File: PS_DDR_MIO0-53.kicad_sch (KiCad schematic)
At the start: 1 part, among them U13 XCZU15EG-2FFVB1156E

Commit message: Stuff
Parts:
- removed U13: XCZU15EG-2FFVB1156E, lib:FFVB1156_XIL-L, symbol XCZU15EG:XCZU15EG-2FFVB1156E
- added U13: XCZU15EG-2FFVB1156E, lib:FFVB1156_XIL-L, symbol XCZU15EG:XCZU15EG-2FFVB1156E
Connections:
- new net DDR_DQS0+: U13.AN18 (PS_DDR_DQS_P0)
- new net DDR_DQS0-: U13.AN19 (PS_DDR_DQS_N0)
- new net DDR_DQS1+: U13.AN21 (PS_DDR_DQS_P1)
- new net DDR_DQS1-: U13.AN22 (PS_DDR_DQS_N1)
- new net ETH_CLK: U13.L23 (PS_MIO38)
- new net ETH_RXD0: U13.K24 (PS_MIO43)
- new net ETH_RXD1: U13.N24 (PS_MIO44)
- new net ETH_RXD2: U13.P24 (PS_MIO45)
- new net ETH_RXD3: U13.J25 (PS_MIO46)
- new net ETH_TXD0: U13.N23 (PS_MIO39)
- new net ETH_TXD1: U13.M23 (PS_MIO40)
- new net ETH_TXD2: U13.J24 (PS_MIO41)
- new net ETH_TXD3: U13.M24 (PS_MIO42)
- new net SD_CLK: U13.AD20 (PS_MIO22)
- new net SD_CMD: U13.AF18 (PS_MIO21)
- new net SD_DATA0: U13.AK17 (PS_MIO13)
- new net SD_DATA1: U13.AL16 (PS_MIO14)
- new net SD_DATA2: U13.AN16 (PS_MIO15)
- new net SD_DATA3: U13.AM16 (PS_MIO16)
- new net SD_DATA4: U13.AP16 (PS_MIO17)
- new net SD_DATA5: U13.AE18 (PS_MIO18)
- new net SD_DATA6: U13.AL17 (PS_MIO19)
- new net SD_DATA7: U13.AD18 (PS_MIO20)
- new net UART0_RX: U13.AL15 (PS_MIO6)
- new net UART0_TX: U13.AD17 (PS_MIO7)
- new net UART1_RX: U13.AE17 (PS_MIO8)
- new net UART1_TX: U13.AP15 (PS_MIO9)

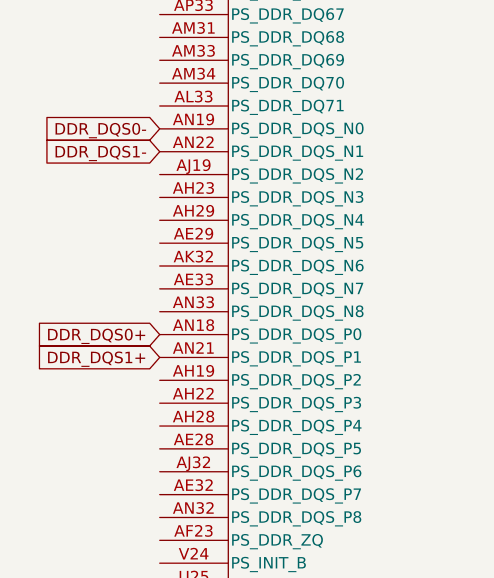
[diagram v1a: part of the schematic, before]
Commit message: DDR4 data lines
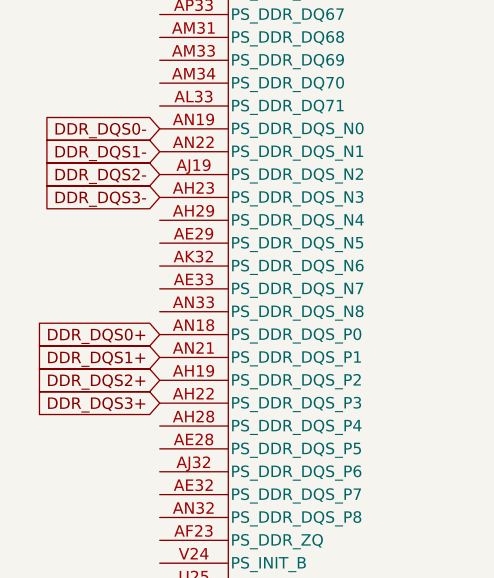
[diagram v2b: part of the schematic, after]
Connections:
- net DDR_DQS2+: now reaches U13.AH19 (PS_DDR_DQS_P2)
- net DDR_DQS3+: now reaches U13.AH22 (PS_DDR_DQS_P3)
- net DDR_DQS3-: now reaches U13.AH23 (PS_DDR_DQS_N3)
- net DDR_DQS2-: now reaches U13.AJ19 (PS_DDR_DQS_N2)
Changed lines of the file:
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@@
+    )
+  )
+  (global_label "DDR_DQS3-" (shape input) (at 87.63 101.6 180) (fields_autoplaced)
+    (effects (font (size 1.27 1.27)) (justify right))
+    (property "Intersheetrefs" "${INTERSHEET_REFS}" (at 73.3547 101.6 0)
+      (effects (font (size 1.27 1.27)) (justify right) hide)
     )
   )
@@
     )
   )
+  (global_label "DDR_DQS2-" (shape input) (at 87.63 99.06 180) (fields_autoplaced)
+    (effects (font (size 1.27 1.27)) (justify right))
+    (property "Intersheetrefs" "${INTERSHEET_REFS}" (at 73.3547 99.06 0)
+      (effects (font (size 1.27 1.27)) (justify right) hide)
+    )
+  )
   (global_label "SD_DATA1" (shape input) (at 153.67 53.34 0) (fields_autoplaced)
     (effects (font (size 1.27 1.27)) (justify left))
@@
     (property "Intersheetrefs" "${INTERSHEET_REFS}" (at 165.8891 33.02 0)
       (effects (font (size 1.27 1.27)) (justify left) hide)
+    )
+  )
+  (global_label "DDR_DQS3+" (shape input) (at 87.63 124.46 180) (fields_autoplaced)
+    (effects (font (size 1.27 1.27)) (justify right))
+    (property "Intersheetrefs" "${INTERSHEET_REFS}" (at 73.3547 124.46 0)
+      (effects (font (size 1.27 1.27)) (justify right) hide)
     )
   )
@@
     )
   )
+  (global_label "DDR_DQS2+" (shape input) (at 87.63 121.92 180) (fields_autoplaced)
+    (effects (font (size 1.27 1.27)) (justify right))
+    (property "Intersheetrefs" "${INTERSHEET_REFS}" (at 73.3547 121.92 0)
+      (effects (font (size 1.27 1.27)) (justify right) hide)
+    )
+  )
